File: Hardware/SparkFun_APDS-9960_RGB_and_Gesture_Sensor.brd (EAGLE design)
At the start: 15.2 x 20.3 mm, 19 parts, among them U1 APDS-9960

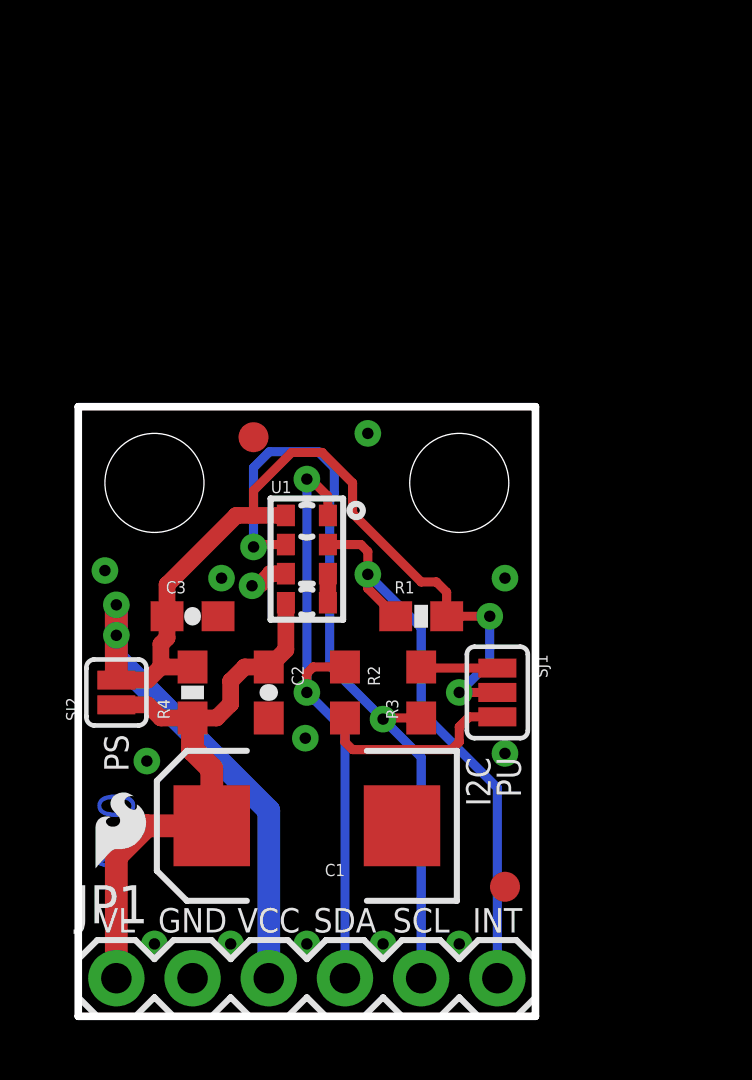
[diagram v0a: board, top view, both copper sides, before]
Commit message: Suggestions For Possible Board Revision
I have a few suggestions to make this board work better in my
application.
I'm a noob with GitHub, so I appologise if I'm doing this wrong.

Changes:
1) Rotate and relocate sensor as close as possible to edge of board.
Reason: I want to be able to put this sensor board into an enclosure
next to an LCD. The sensor needs to be as close to the LCD for both to
fit in the window.

2) Add location on back of board for large electrolytic capacitor.
Reason: placing the capacitor behind the sensor improves packaging
options for the board and sensor.

3) Added voltage regulator and level shifting components to make the
board 5V safe.
Reason: Easier to integrate with Arduinos and other 5V micros.
Note: In my understanding of the APDS datasheet the sensor can pull up
to 790mA. Because of this, a 1A regulator was selected, MCP1826T. Device
and footprint created in my Eagle library
(https://github.com/akreager/ATK_Engineering-Eagle_Library). I2C level
shifter design "borrowed" from SparkFun logic level shifter board.

4) (Least important) Attempted to add provisions to be able to break
board into two pieces and reconnet with jumper wires.
Reason: Packaging.

5) Moved fiduciary marks and silkscreens, added mounting holes, changed
revision in the board to v10x1 (my way to signify an unapproved
revision).
Reason: clearance; revision tracking.
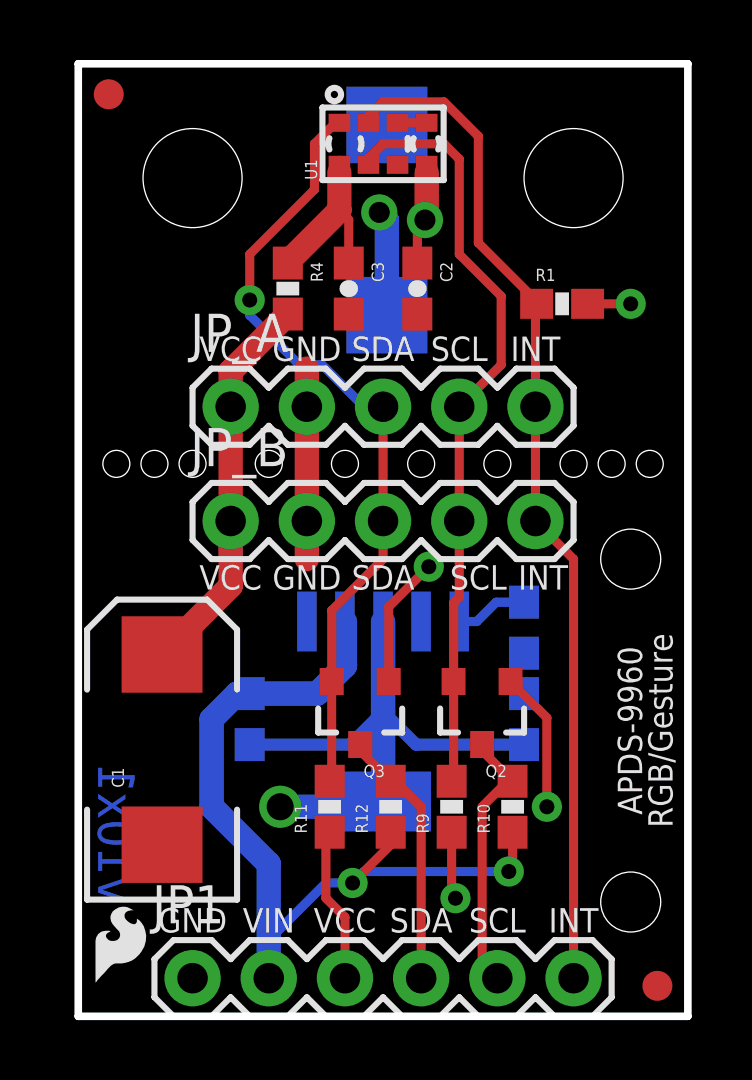
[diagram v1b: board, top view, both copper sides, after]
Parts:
- removed LOGO2: OSHW-LOGOS, SparkFun-Aesthetics:OSHW-LOGO-S
- removed R2, R3: 4.7k, SparkFun-Resistors:0603
- removed SJ1: (no value), SparkFun-Passives:SJ_3_PASTE1&2&3
- removed SJ2: SOLDERJUMPERNC, SparkFun-Retired:SJ_2S
- removed U$1: SFE_LOGO_NAME_FLAME.1_INCH, SparkFun-Aesthetics:SFE_LOGO_NAME_FLAME_.1
- added BACK_CAP: 100uF, SparkFun-Capacitors:EIA7343
- added C4: 1.0uF, SparkFun-Capacitors:0603-CAP
- added C5: 4.7uF, SparkFun-Capacitors:0603-CAP
- added JP_A, JP_B: (no value), SparkFun-Connectors:1X05
- added Q2, Q3: BSS138, SparkFun:SOT23-3
- added R10, R11, R12, R9: 10K, SparkFun:0603-RES
- added R13: 100K, SparkFun:0603-RES
- added U$2: MCP1826TMCP1826T, ATK_lib:SOP-223-5
- moved C2 14.3 mm to (11.3, 24.3)
- moved U1 14.1 mm to (10.2, 29.1), turned to 90 degrees
- moved R4 13.8 mm to (6.99, 24.3), turned to 270 degrees
- moved FID2 12.4 mm to (1.02, 30.7)
- moved C3 12.1 mm to (9.02, 24.3), turned to 270 degrees
- moved R1 11.4 mm to (16.1, 23.7)
- moved STANDOFF2 10.9 mm to (16.5, 27.9)
- moved STANDOFF1 10.2 mm to (3.81, 27.9)
- moved FID1 6.06 mm to (19.3, 1.02)
- moved C1 5.45 mm to (2.79, 8.89), turned to 90 degrees
- moved LOGO1 3.81 mm to (0.25, 0.76)
- moved JP1 2.54 mm to (3.81, 1.27)
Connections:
- removed net N$2: R3.2, SJ1.1
- removed net VL: C1.A, C2.1, JP1.1, R4.1, SJ2.1, U1.5
- new net N$6: R13.2, U$2.5
- new net SCL_5V: JP1.5, Q2.3, R10.2
- new net SDA_5V: JP1.4, Q3.3, R12.2
- new net VIN: C5.2, JP1.2, R10.1, R12.1, U$2.2
- net GND: now also BACK_CAP.C, C4.2, C5.1, JP1.1, JP_A.2, JP_B.2, U$2.3, U$2.6; no longer JP1.2
- net INT: now also JP_A.5, JP_B.5
- net N$1: now also C3.1, R4.1, U1.8; no longer R2.2, SJ1.3
- net SCL: now also JP_A.4, JP_B.4, Q2.2, R9.2; no longer JP1.5, R3.1
- net SDA: now also JP_A.3, JP_B.3, Q3.2, R11.2; no longer JP1.4, R2.1
- net VCC: now also BACK_CAP.A, C1.A, C2.1, C4.1, JP_A.1, JP_B.1, Q2.1, Q3.1, R11.1, R13.1, R9.1, U$2.4, U1.5; no longer C3.1, SJ1.2, SJ2.2, U1.8
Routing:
- net VIN: track 0.00 -> 28.6 mm, vias 0 -> 2
- net GND: track 1.00 -> 29.4 mm, vias 13 -> 2
- net VL: track 20.3 -> 0.00 mm
- net INT: track 19.2 -> 34.0 mm, vias 1 -> 0
- net SCL_5V: track 0.00 -> 8.94 mm
- net SDA_5V: track 0.00 -> 8.73 mm
- net VCC: track 44.3 -> 35.7 mm, vias 4 -> 5
- net SDA: track 20.7 -> 26.8 mm, vias 2 -> 1
- net N$2: track 2.56 -> 0.00 mm
- net N$6: track 0.00 -> 2.43 mm
- net SCL: track 26.5 -> 25.7 mm, vias 2 -> 0
- net N$1: track 6.74 -> 5.88 mm
- added copper zone on layer 16, net VCC
- removed copper zone on layer 16, net GND
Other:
- board size 15.2 x 20.3 mm -> 20.3 x 31.8 mm
- board text added: "VIN"
- board text added: "v10x1"
- board text removed: "I2C"
- board text removed: "PS"
- board text removed: "PU"
- board text removed: "VL"
- board text removed: "v10"
